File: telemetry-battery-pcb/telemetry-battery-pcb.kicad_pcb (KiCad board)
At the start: 2 copper layers, 94.9 x 65.1 mm, 110 parts, among them J1 Network Connector, J2 STDC14, J3 CONN_360410_MZC, J4 DS18B20, J5 CONN_360410_MZC, Q1 NMOS, Q2 PMOS, Q4 NMOS, SW1 SW_Push, U1 LD39050PU33R, U2 STM32G474RBT6, U3 SN65HVD230, U4 LTC2944, U5 XR76208, U6 M24C02-WMN, U7 TPS1HTC30-Q1, U8 DS2484Q, Y1 8MHz

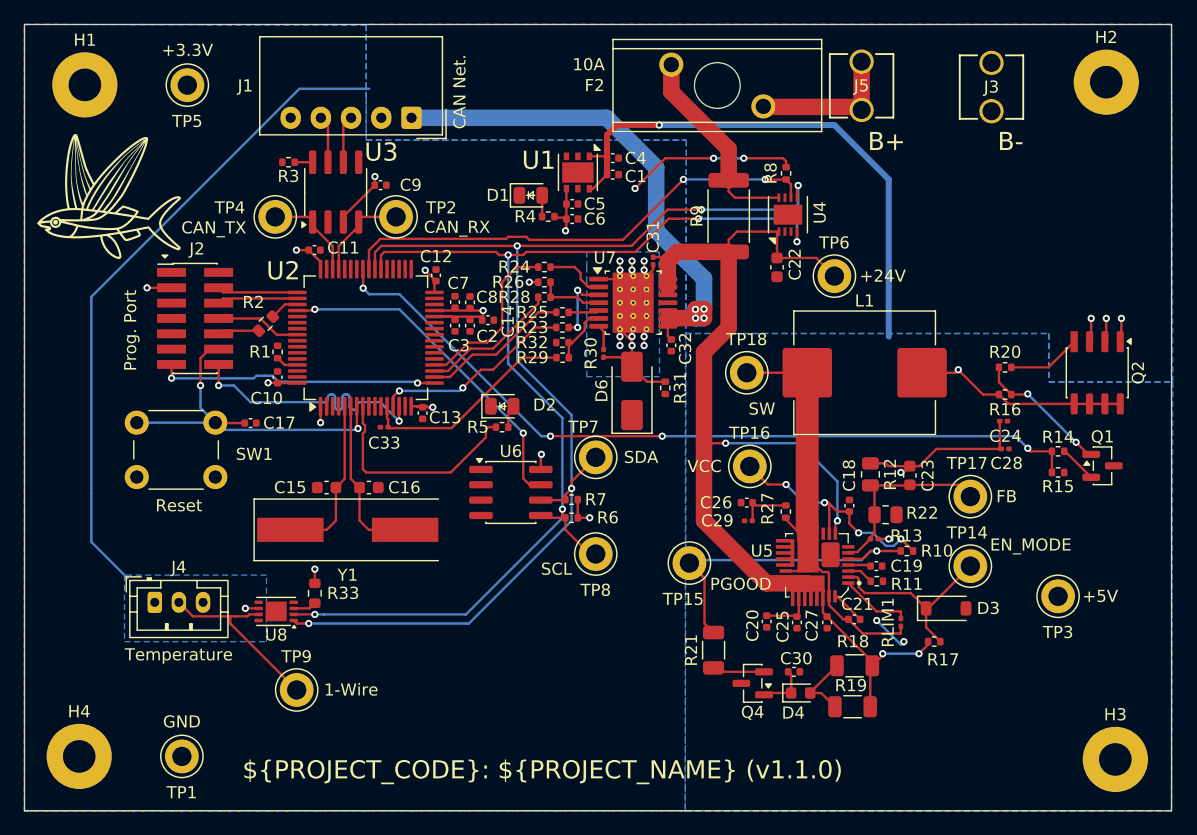
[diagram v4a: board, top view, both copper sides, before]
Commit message: telemetry-battery-pcb: round pcb dimensions
- Moved edge cuts and planes
- Moved mounting holes
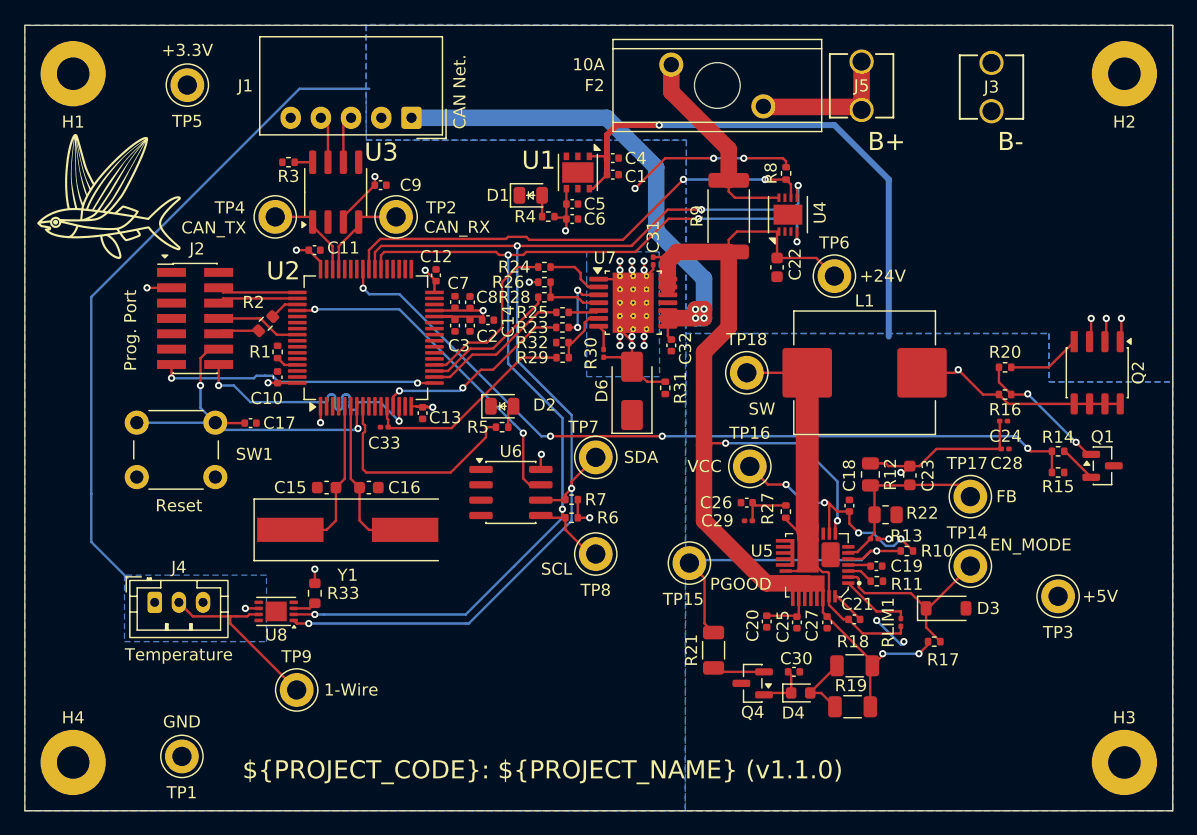
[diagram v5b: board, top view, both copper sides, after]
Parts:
- moved H2 1.66 mm to (135.5, 25.5)
- moved H1 1.34 mm to (48.5, 25.5)
- moved H3 0.79 mm to (135.5, 82.5)
- moved H4 0.71 mm to (48.5, 82.5)
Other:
- board size 94.9 x 65.1 mm -> 95 x 65 mm
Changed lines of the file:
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@@
 		(tenting front back)
 		(pcbplotparams
-			(layerselection 0x00000000_00000000_55555555_5755f5ff)
+			(layerselection 0x00000000_00000000_55555555_57575550)
 			(plot_on_all_layers_selection 0x00000000_00000000_00000000_00000000)
 			(disableapertmacros no)
@@
 			(dashed_line_gap_ratio 3.000000)
 			(svgprecision 4)
-			(plotframeref no)
+			(plotframeref yes)
 			(mode 1)
 			(useauxorigin no)
@@
 			(pdf_back_fp_property_popups yes)
 			(pdf_metadata yes)
-			(pdf_single_document no)
+			(pdf_single_document yes)
 			(dxfpolygonmode yes)
 			(dxfimperialunits yes)
@@
 			(crossoutdnponfab yes)
 			(subtractmaskfromsilk no)
-			(outputformat 1)
+			(outputformat 4)
 			(mirror no)
-			(drillshape 1)
+			(drillshape 2)
 			(scaleselection 1)
-			(outputdirectory "")
+			(outputdirectory "./")
 		)
 	)
@@
 	(footprint "MountingHole:MountingHole_2.7mm_Pad"
 		(layer "F.Cu")
-		(at 49.47 26.425)
+		(at 48.5 25.5)
 		(descr "Mounting Hole 2.7mm")
 		(tags "mounting hole 2.7mm")
 		(property "Reference" "H1"
-			(at 0 -3.7 0)
+			(at 0 4 0)
 			(layer "F.SilkS")
 			(effects
@@
 	(footprint "MountingHole:MountingHole_2.7mm_Pad"
 		(layer "F.Cu")
-		(at 49 82)
+		(at 48.5 82.5)
 		(descr "Mounting Hole 2.7mm")
 		(tags "mounting hole 2.7mm")
@@
 	(footprint "MountingHole:MountingHole_2.7mm_Pad"
 		(layer "F.Cu")
-		(at 134.75 82.25)
+		(at 135.5 82.5)
 		(descr "Mounting Hole 2.7mm")
 		(tags "mounting hole 2.7mm")
@@
 	(footprint "MountingHole:MountingHole_2.7mm_Pad"
 		(layer "F.Cu")
-		(at 134 26.2)
+		(at 135.5 25.5)
 		(descr "Mounting Hole 2.7mm")
 		(tags "mounting hole 2.7mm")
 		(property "Reference" "H2"
-			(at 0 -3.7 0)
+			(at 0 4 0)
 			(layer "F.SilkS")
 			(effects
@@
 	)
 	(gr_rect
-		(start 44.47 21.425)
-		(end 139.4 86.5)
+		(start 44.5 21.5)
+		(end 139.5 86.5)
 		(stroke
 			(width 0.05)
@@
 		(polygon
 			(pts
-				(xy 139.4 86.5) (xy 44.47 86.525) (xy 44.47 21.425) (xy 139.4 21.425)
+				(xy 139.5 86.5) (xy 44.5 86.5) (xy 44.5 21.5) (xy 139.5 21.5)
 			)
 		)
@@
 		(polygon
 			(pts
-				(xy 44.47 21.425) (xy 72.75 21.491375) (xy 72.75 27.472389) (xy 72.762352 31) (xy 75.787445 31)
-				(xy 99.25 31) (xy 99.156141 86.525) (xy 44.47 86.525)
+				(xy 44.5 21.5) (xy 72.75 21.491375) (xy 72.75 27.472389) (xy 72.762352 31) (xy 75.787445 31) (xy 99.25 31)
+				(xy 99.156141 86.525) (xy 44.5 86.5)
 			)
 		)
@@
 		(polygon
 			(pts
-				(xy 139.4 21.425) (xy 72.75 21.425) (xy 72.75 31) (xy 99.25 31) (xy 99.175 47) (xy 129.25 47) (xy 129.25 51)
+				(xy 139.5 21.5) (xy 72.75 21.425) (xy 72.75 31) (xy 99.25 31) (xy 99.175 47) (xy 129.25 47) (xy 129.25 51)
 				(xy 139.5 51)
 			)
@@
 		(polygon
 			(pts
-				(xy 139.4 86.5) (xy 99.156141 86.525) (xy 99.175 47) (xy 129.25 47) (xy 129.25 51) (xy 139.5 51)
+				(xy 139.5 86.5) (xy 99.156141 86.525) (xy 99.175 47) (xy 129.25 47) (xy 129.25 51) (xy 139.5 51)
 			)
 		)

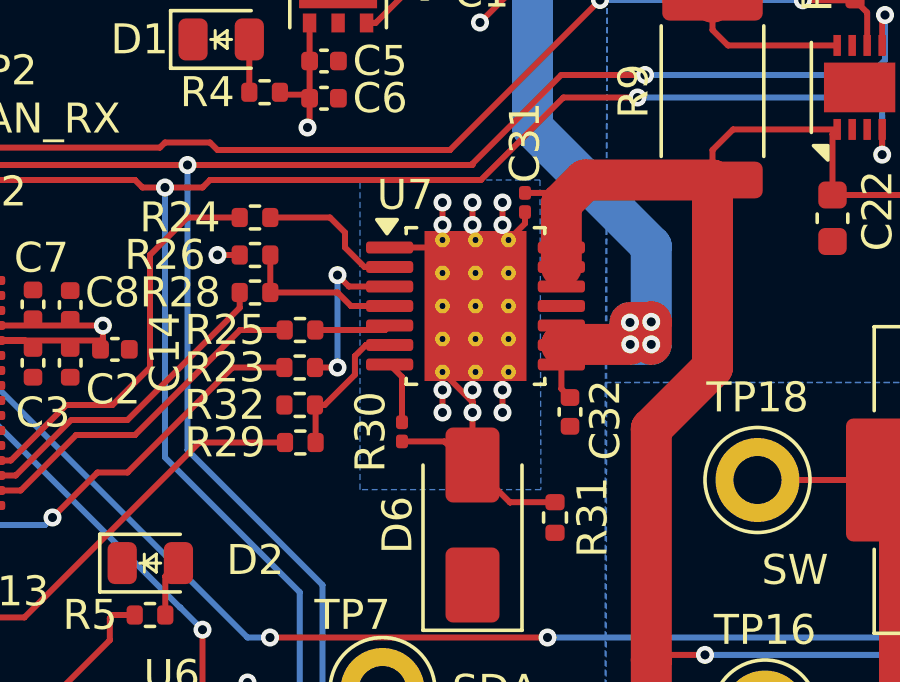
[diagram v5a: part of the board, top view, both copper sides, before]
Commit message: telemetry-battery-pcb: add GND_L plane
For better thermal relief.
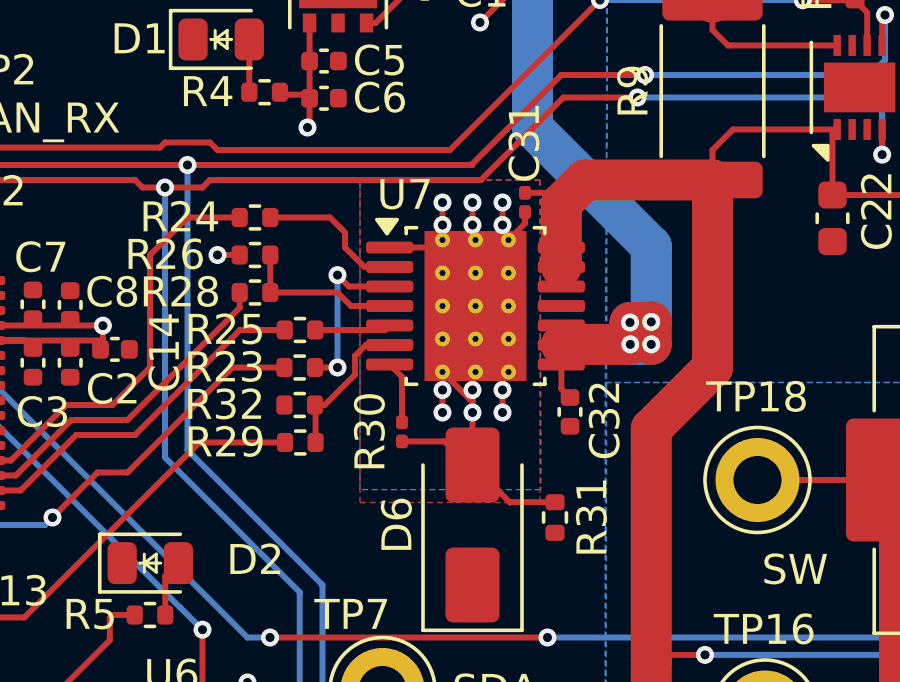
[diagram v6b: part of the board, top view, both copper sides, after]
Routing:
- added copper zone on F.Cu, net /GND_L
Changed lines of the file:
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@@
+	)
+	(zone
+		(net 96)
+		(net_name "/GND_L")
+		(layer "F.Cu")
+		(hatch edge 0.5)
+		(priority 6)
+		(connect_pads yes
+			(clearance 0.18)
+		)
+		(min_thickness 0.25)
+		(filled_areas_thickness no)
+		(fill yes
+			(thermal_gap 0.5)
+			(thermal_bridge_width 0.5)
+		)
+		(polygon
+			(pts
+				(xy 91 51) (xy 97 51) (xy 97 40.25) (xy 91 40.25)
+			)
+		)
 	)
 	(zone
@@
 		(hatch edge 0.5)
 		(priority 4)
-		(connect_pads
+		(connect_pads yes
 			(clearance 0.18)
 		)
